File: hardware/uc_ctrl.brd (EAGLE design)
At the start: 62.5 x 23 mm, 46 parts, among them Q4 si2305cd, Q7 si2305cd, T1 BC846, T3 BC846, U1 3vLDO, Y1 32768Hz CFPX-217 12.5pF

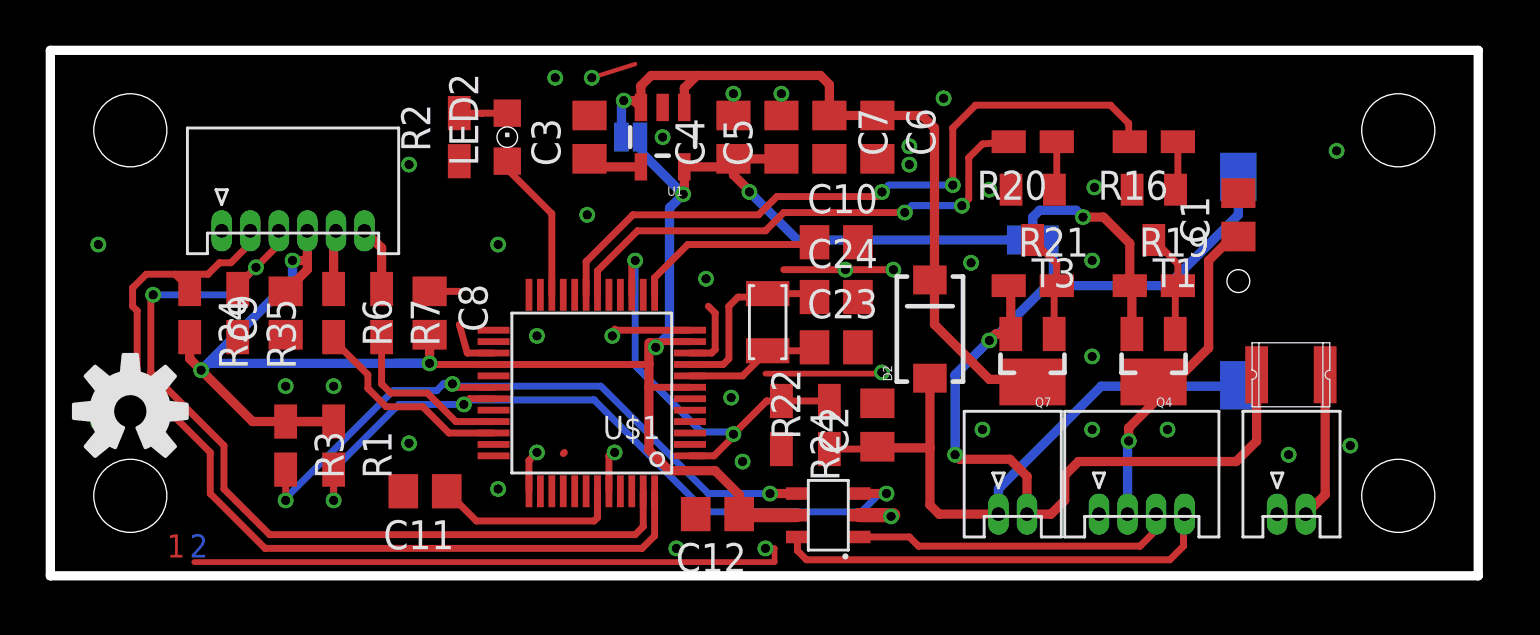
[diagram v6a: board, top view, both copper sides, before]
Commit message: add 0.5mm to board width
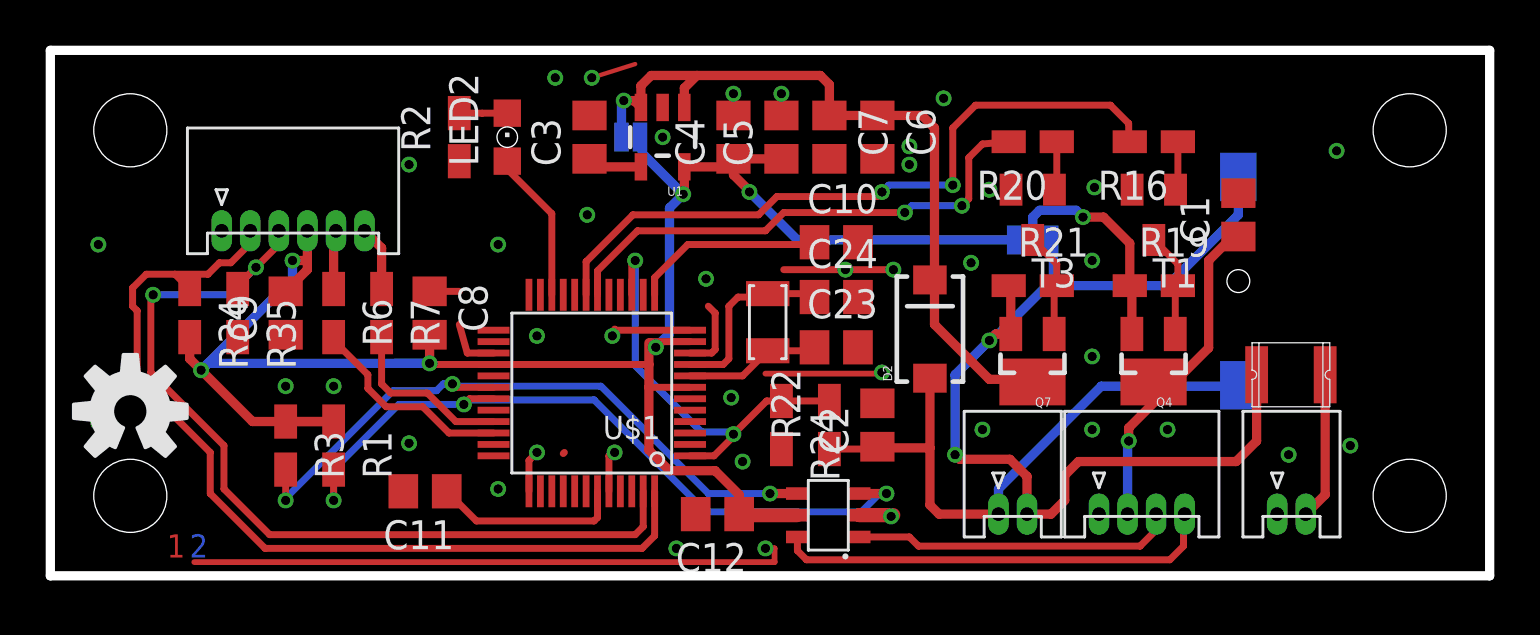
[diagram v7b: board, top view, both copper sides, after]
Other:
- board size 62.5 x 23 mm -> 63 x 23 mm
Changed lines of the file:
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@@
 <layer number="42" name="bRestrict" color="1" fill="10" visible="yes" active="yes"/>
 <layer number="43" name="vRestrict" color="2" fill="10" visible="no" active="yes"/>
-<layer number="44" name="Drills" color="7" fill="1" visible="no" active="yes"/>
-<layer number="45" name="Holes" color="7" fill="1" visible="no" active="yes"/>
-<layer number="46" name="Milling" color="3" fill="1" visible="no" active="yes"/>
+<layer number="44" name="Drills" color="7" fill="1" visible="yes" active="yes"/>
+<layer number="45" name="Holes" color="7" fill="1" visible="yes" active="yes"/>
+<layer number="46" name="Milling" color="3" fill="1" visible="yes" active="yes"/>
 <layer number="47" name="Measures" color="7" fill="1" visible="no" active="yes"/>
-<layer number="48" name="Document" color="7" fill="1" visible="no" active="yes"/>
+<layer number="48" name="Document" color="7" fill="1" visible="yes" active="yes"/>
 <layer number="49" name="Reference" color="7" fill="1" visible="no" active="yes"/>
 <layer number="50" name="dxf" color="7" fill="1" visible="no" active="yes"/>
-<layer number="51" name="tDocu" color="7" fill="1" visible="no" active="yes"/>
-<layer number="52" name="bDocu" color="7" fill="1" visible="no" active="yes"/>
+<layer number="51" name="tDocu" color="7" fill="1" visible="yes" active="yes"/>
+<layer number="52" name="bDocu" color="7" fill="1" visible="yes" active="yes"/>
 <layer number="53" name="tGND_GNDA" color="7" fill="9" visible="no" active="no"/>
 <layer number="54" name="bGND_GNDA" color="1" fill="9" visible="no" active="no"/>
@@
 <board>
 <plain>
-<wire x1="0" y1="0" x2="62.5" y2="0" width="0.4064" layer="20"/>
-<wire x1="62.5" y1="0" x2="62.5" y2="23" width="0.4064" layer="20"/>
-<wire x1="62.5" y1="23" x2="0" y2="23" width="0.4064" layer="20"/>
+<wire x1="0" y1="0" x2="63" y2="0" width="0.4064" layer="20"/>
+<wire x1="63" y1="0" x2="63" y2="23" width="0.4064" layer="20"/>
+<wire x1="63" y1="23" x2="0" y2="23" width="0.4064" layer="20"/>
 <wire x1="0" y1="23" x2="0" y2="0" width="0.4064" layer="20"/>
 <text x="30.2" y="1.7" size="1.01" layer="109" font="vector" ratio="15" rot="MR0"></text>
-<hole x="59" y="3.5" drill="3.2"/>
+<hole x="59.5" y="3.5" drill="3.2"/>
 <wire x1="54.2" y1="17.5" x2="61.6" y2="17.5" width="0.254" layer="108"/>
 <wire x1="61.6" y1="6.3" x2="56.7" y2="6.3" width="0.254" layer="108"/>
@@
 <wire x1="53.4" y1="16.3" x2="61.6" y2="16.3" width="0.1" layer="108"/>
 <hole x="3.5" y="3.5" drill="3.2"/>
-<hole x="59" y="19.5" drill="3.2"/>
+<hole x="59.5" y="19.5" drill="3.2"/>
 <hole x="3.5" y="19.5" drill="3.2"/>
 <hole x="20" y="19.2" drill="0.9"/>
@@
 <vertex x="0" y="23"/>
 <vertex x="0" y="0"/>
-<vertex x="62.5" y="0"/>
-<vertex x="62.5" y="23"/>
+<vertex x="63" y="0"/>
+<vertex x="63" y="23"/>
 </polygon>
 <polygon width="0.3048" layer="16" isolate="0.3048">
 <vertex x="0" y="23"/>
 <vertex x="0" y="0"/>
-<vertex x="62.5" y="0"/>
-<vertex x="62.5" y="23"/>
+<vertex x="63" y="0"/>
+<vertex x="63" y="23"/>
 </polygon>
 <contactref element="C1" pad="2"/>

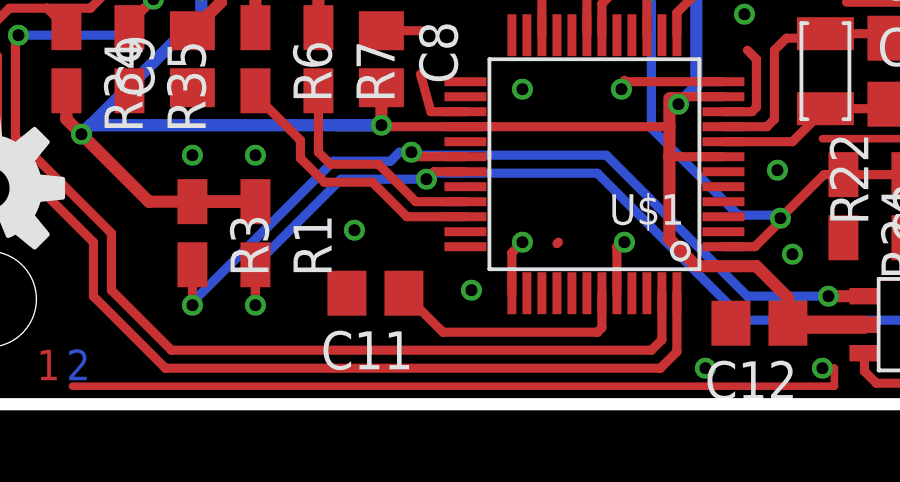
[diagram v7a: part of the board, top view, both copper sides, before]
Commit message: unused pin tweaks
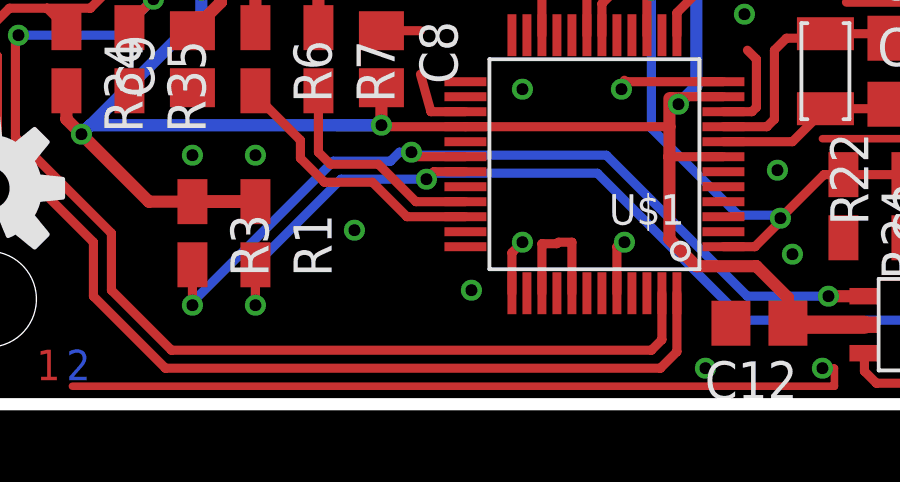
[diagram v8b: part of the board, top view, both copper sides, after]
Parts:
- removed C11: 220nF, rcl:C0805
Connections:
- removed net 41: U$1.41
- removed net N$7: C11.1, U$1.43
- new net 43: U$1.43
- net GND: now also U$1.39, U$1.41; no longer C11.2
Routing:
- net N$7: track 8.35 -> 0.00 mm
- net GND: track 55.3 -> 59.6 mm
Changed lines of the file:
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@@
 <element name="U$1" library="TI_MSP430_v16" package="PT48" value="F55[0/1]X---PT48" x="23.7" y="8" rot="R180"/>
 <element name="C10" library="rcl" package="C0805" value="470nF" x="34.4" y="14.6"/>
-<element name="C11" library="rcl" package="C0805" value="220nF" x="16.4" y="3.7" rot="R180"/>
 <element name="R6" library="rcl" package="R0805W" value="4.7k" x="12.4" y="11.5" rot="R270"/>
 <element name="R7" library="rcl" package="R0805W" value="4.7k" x="14.5" y="11.5" rot="R270"/>
@@
 <contactref element="C1" pad="2"/>
 <contactref element="C2" pad="2"/>
-<contactref element="C11" pad="2"/>
 <contactref element="U1" pad="2"/>
 <contactref element="C3" pad="2"/>
@@
 <via x="15.7" y="18" extent="1-16" drill="0.4"/>
 <via x="19.6" y="3.8" extent="1-16" drill="0.4"/>
+<contactref element="U$1" pad="39"/>
+<contactref element="U$1" pad="41"/>
+<wire x1="22.95" y1="3.7" x2="22.95" y2="5.4" width="0.3048" layer="1"/>
+<wire x1="22.95" y1="5.4" x2="22.5" y2="5.4" width="0.3048" layer="1"/>
+<wire x1="21.95" y1="3.7" x2="21.95" y2="5.35" width="0.3048" layer="1"/>
+<wire x1="21.95" y1="5.35" x2="22.45" y2="5.35" width="0.3048" layer="1"/>
 </signal>
 <signal name="N$6">
@@
 <wire x1="27.9" y1="14.5" x2="33.35" y2="14.5" width="0.3048" layer="1"/>
 <wire x1="33.35" y1="14.5" x2="33.45" y2="14.6" width="0.3048" layer="1" curve="90"/>
-</signal>
-<signal name="N$7">
-<contactref element="U$1" pad="43"/>
-<contactref element="C11" pad="1"/>
-<wire x1="23.95" y1="3.7" x2="23.95" y2="2.55" width="0.3048" layer="1"/>
-<wire x1="23.95" y1="2.55" x2="23.8" y2="2.4" width="0.3048" layer="1"/>
-<wire x1="23.8" y1="2.4" x2="18.65" y2="2.4" width="0.3048" layer="1"/>
-<wire x1="18.65" y1="2.4" x2="17.35" y2="3.7" width="0.3048" layer="1"/>
 </signal>
 <signal name="N$11">
@@
 <contactref element="U$1" pad="46"/>
 </signal>
-<signal name="41">
-<contactref element="U$1" pad="41"/>
-</signal>
 <signal name="UC_POW">
 <contactref element="Q4" pad="3"/>
@@
 <wire x1="12.4" y1="4.6475" x2="12.4" y2="3.3" width="0.3048" layer="1"/>
 </signal>
+<signal name="43">
+<contactref element="U$1" pad="43"/>
+</signal>
 </signals>
